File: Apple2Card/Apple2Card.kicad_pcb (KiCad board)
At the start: 2 copper layers, 160 x 78.2 mm, 69 parts, among them J1 ICSP, J2 Conn_01x25, J3 Conn_01x25, J4 Conn_01x16, J5 SERCON, J6 WIZNET 5500, SW1 SW_Push, U1 ATmega328P-P, U2 74HCT32, U3 74HCT00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

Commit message: JLCPCB order 2022-06-15
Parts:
- moved JP10 0.14 mm to (104.4, 34.9)
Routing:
- net GND: track 217.9 -> 241.2 mm
- net Net-(D8-Pad1): track 111.7 -> 112.2 mm
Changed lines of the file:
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@@
       (effects (font (size 1 1) (thickness 0.15)))
     )
-    (fp_text user "K" (at 0 -1.8) (layer "F.Fab")
+    (fp_text user "K" (at 0 -1.8) (layer "F.Fab") hide
       (effects (font (size 1 1) (thickness 0.15)))
     )
@@
   )
   (footprint "Connector_PinHeader_2.54mm:PinHeader_1x02_P2.54mm_Vertical" (layer "F.Cu")
-    (at 104.445 35 90)
+    (at 104.445 34.86 90)
     (descr "Through hole straight pin header, 1x02, 2.54mm pitch, single row")
     (tags "Through hole pin header THT 1x02 2.54mm single row")
@@
   (segment (start 168.59 83.16) (end 115.3 83.16) (width 0.35) (layer "F.Cu") (net 26))
   (segment (start 71.91 63.75) (end 72.64 63.75) (width 0.35) (layer "F.Cu") (net 26))
-  (segment (start 133.79 57.56) (end 137.59 57.56) (width 0.35) (layer "F.Cu") (net 26))
   (segment (start 138.97 58.94) (end 138.97 58.96) (width 0.35) (layer "F.Cu") (net 26))
   (segment (start 69.21 62.36) (end 69.64 61.93) (width 0.35) (layer "F.Cu") (net 26))
   (segment (start 123.12 69.65) (end 123.12 68.23) (width 0.35) (layer "F.Cu") (net 26))
+  (segment (start 135.45 57.56) (end 119.23 57.56) (width 0.35) (layer "F.Cu") (net 26))
   (segment (start 180.09 78.51) (end 178.07 80.53) (width 0.35) (layer "F.Cu") (net 26))
   (segment (start 91.275 72.625) (end 102.2 72.625) (width 0.35) (layer "F.Cu") (net 26))
@@
   (segment (start 108.6 89.86) (end 83.34 89.86) (width 0.35) (layer "F.Cu") (net 26))
   (segment (start 56.73 59.856) (end 58.376 58.21) (width 0.35) (layer "F.Cu") (net 26))
+  (segment (start 119.23 57.56) (end 118.44 56.77) (width 0.35) (layer "F.Cu") (net 26))
   (segment (start 102.2 72.625) (end 103.485 71.34) (width 0.35) (layer "F.Cu") (net 26))
   (segment (start 178.07 80.53) (end 171.22 80.53) (width 0.35) (layer "F.Cu") (net 26))
+  (segment (start 118.44 56.77) (end 118.44 56.56) (width 0.35) (layer "F.Cu") (net 26))
   (segment (start 64.38 57.39) (end 65.55 57.39) (width 0.35) (layer "F.Cu") (net 26))
   (segment (start 138.97 58.96) (end 142.81 62.8) (width 0.35) (layer "F.Cu") (net 26))
+  (segment (start 134.11 57.56) (end 135.45 57.56) (width 0.35) (layer "F.Cu") (net 26))
   (segment (start 121.235 71.535) (end 123.12 69.65) (width 0.35) (layer "F.Cu") (net 26))
   (segment (start 69.64 61.48) (end 71.91 63.75) (width 0.35) (layer "F.Cu") (net 26))
+  (segment (start 135.45 57.56) (end 137.59 57.56) (width 0.35) (layer "F.Cu") (net 26))
   (segment (start 123.12 68.23) (end 133.79 57.56) (width 0.35) (layer "F.Cu") (net 26))
   (segment (start 58.376 58.21) (end 63.56 58.21) (width 0.35) (layer "F.Cu") (net 26))
@@
   (segment (start 103.485 71.34) (end 108.08 71.34) (width 0.35) (layer "F.Cu") (net 26))
   (segment (start 87.1 79.6) (end 87.1 76.8) (width 0.35) (layer "F.Cu") (net 26))
+  (segment (start 133.79 57.56) (end 134.11 57.56) (width 0.35) (layer "F.Cu") (net 26))
   (segment (start 81.82 84.88) (end 87.1 79.6) (width 0.35) (layer "F.Cu") (net 26))
+  (segment (start 118.44 56.56) (end 114.41 52.53) (width 0.35) (layer "F.Cu") (net 26))
   (segment (start 115.3 83.16) (end 108.6 89.86) (width 0.35) (layer "F.Cu") (net 26))
   (segment (start 69.64 61.93) (end 69.64 61.48) (width 0.35) (layer "F.Cu") (net 26))
@@
   (segment (start 43.942 37.2) (end 43.804 37.338) (width 0.35) (layer "B.Cu") (net 55))
   (segment (start 43.804 37.338) (end 40.932 37.338) (width 0.35) (layer "B.Cu") (net 55))
-  (segment (start 117.45 84.81) (end 117.45 84.54) (width 0.35) (layer "F.Cu") (net 56))
-  (segment (start 169.82 83.86) (end 171.23 82.45) (width 0.35) (layer "F.Cu") (net 56))
-  (segment (start 117.45 84.54) (end 118.13 83.86) (width 0.35) (layer "F.Cu") (net 56))
-  (segment (start 118.13 83.86) (end 169.82 83.86) (width 0.35) (layer "F.Cu") (net 56))
-  (via (at 171.23 82.45) (size 0.8) (drill 0.4) (layers "F.Cu" "B.Cu") (net 56))
+  (segment (start 117.45 84.54) (end 117.45 84.81) (width 0.35) (layer "F.Cu") (net 56))
+  (segment (start 118.13 83.86) (end 117.45 84.54) (width 0.35) (layer "F.Cu") (net 56))
+  (segment (start 170.73 83.86) (end 118.13 83.86) (width 0.35) (layer "F.Cu") (net 56))
+  (segment (start 171.2 83.39) (end 170.73 83.86) (width 0.35) (layer "F.Cu") (net 56))
+  (via (at 171.2 83.39) (size 0.8) (drill 0.4) (layers "F.Cu" "B.Cu") (net 56))
   (via (at 117.45 84.81) (size 0.8) (drill 0.4) (layers "F.Cu" "B.Cu") (net 56))
-  (segment (start 187.62 73.14) (end 184.84 73.14) (width 0.35) (layer "B.Cu") (net 56))
+  (segment (start 182.61 75.37) (end 184.84 73.14) (width 0.35) (layer "B.Cu") (net 56))
   (segment (start 101.31 91.89) (end 100.83 92.37) (width 0.35) (layer "B.Cu") (net 56))
-  (segment (start 182.61 75.37) (end 172.99 75.37) (width 0.35) (layer "B.Cu") (net 56))
-  (segment (start 184.84 73.14) (end 182.61 75.37) (width 0.35) (layer "B.Cu") (net 56))
+  (segment (start 171.2 77.16) (end 172.99 75.37) (width 0.35) (layer "B.Cu") (net 56))
+  (segment (start 187.62 73.14) (end 187.62 63.917) (width 0.35) (layer "B.Cu") (net 56))
   (segment (start 117.45 86.6) (end 112.16 91.89) (width 0.35) (layer "B.Cu") (net 56))
   (segment (start 117.45 84.81) (end 117.45 86.6) (width 0.35) (layer "B.Cu") (net 56))
-  (segment (start 185.669 61.966) (end 187.62 63.917) (width 0.35) (layer "B.Cu") (net 56))
-  (segment (start 172.99 75.37) (end 171.2 77.16) (width 0.35) (layer "B.Cu") (net 56))
-  (segment (start 171.2 82.42) (end 171.23 82.45) (width 0.35) (layer "B.Cu") (net 56))
+  (segment (start 184.84 73.14) (end 187.62 73.14) (width 0.35) (layer "B.Cu") (net 56))
+  (segment (start 172.99 75.37) (end 182.61 75.37) (width 0.35) (layer "B.Cu") (net 56))
   (segment (start 112.16 91.89) (end 101.31 91.89) (width 0.35) (layer "B.Cu") (net 56))
-  (segment (start 171.2 77.16) (end 171.2 82.42) (width 0.35) (layer "B.Cu") (net 56))
-  (segment (start 187.62 63.917) (end 187.62 73.14) (width 0.35) (layer "B.Cu") (net 56))
+  (segment (start 171.2 83.39) (end 171.2 77.16) (width 0.35) (layer "B.Cu") (net 56))
+  (segment (start 187.62 63.917) (end 185.669 61.966) (width 0.35) (layer "B.Cu") (net 56))
   (segment (start 100.83 92.37) (end 100.19 92.37) (width 0.35) (layer "B.Cu") (net 56))
   (segment (start 65.02 48.51) (end 60.96 52.57) (width 0.35) (layer "B.Cu") (net 57))
@@
   (segment (start 102.8 29.11) (end 103.59 29.9) (width 0.35) (layer "B.Cu") (net 80))
   (segment (start 92.84 29.8) (end 93.53 29.11) (width 0.35) (layer "B.Cu") (net 80))
-  (segment (start 103.59 34.145) (end 104.445 35) (width 0.35) (layer "B.Cu") (net 80))
+  (segment (start 103.59 34.005) (end 104.445 34.86) (width 0.35) (layer "B.Cu") (net 80))
+  (segment (start 103.59 31.21) (end 103.59 34.005) (width 0.35) (layer "B.Cu") (net 80))
   (segment (start 92.84 38.32) (end 92.84 29.8) (width 0.35) (layer "B.Cu") (net 80))
   (segment (start 93.53 29.11) (end 102.8 29.11) (width 0.35) (layer "B.Cu") (net 80))
-  (segment (start 103.59 31.21) (end 103.59 34.145) (width 0.35) (layer "B.Cu") (net 80))
   (segment (start 103.59 29.9) (end 103.59 31.21) (width 0.35) (layer "B.Cu") (net 80))
   (segment (start 82.906 80.62) (end 91.426 89.14) (width 0.35) (layer "B.Cu") (net 81))
@@
   (segment (start 117.48 36.72) (end 119.44 36.72) (width 0.35) (layer "B.Cu") (net 123))
   (segment (start 119.44 36.72) (end 121.235 38.515) (width 0.35) (layer "B.Cu") (net 123))
-  (segment (start 113.56 34.8) (end 107.185 34.8) (width 0.35) (layer "B.Cu") (net 123))
   (segment (start 113.66 34.7) (end 113.56 34.8) (width 0.35) (layer "B.Cu") (net 123))
-  (segment (start 107.185 34.8) (end 106.985 35) (width 0.35) (layer "B.Cu") (net 123))
+  (segment (start 113.56 34.8) (end 107.045 34.8) (width 0.35) (layer "B.Cu") (net 123))
+  (segment (start 107.045 34.8) (end 106.985 34.86) (width 0.35) (layer "B.Cu") (net 123))
   (segment (start 42.164 48.768) (end 42.214 48.818) (width 0.35) (layer "F.Cu") (net 124))
   (segment (start 45.72 73.96) (end 45.716 73.964) (width 0.35) (layer "F.Cu") (net 124))

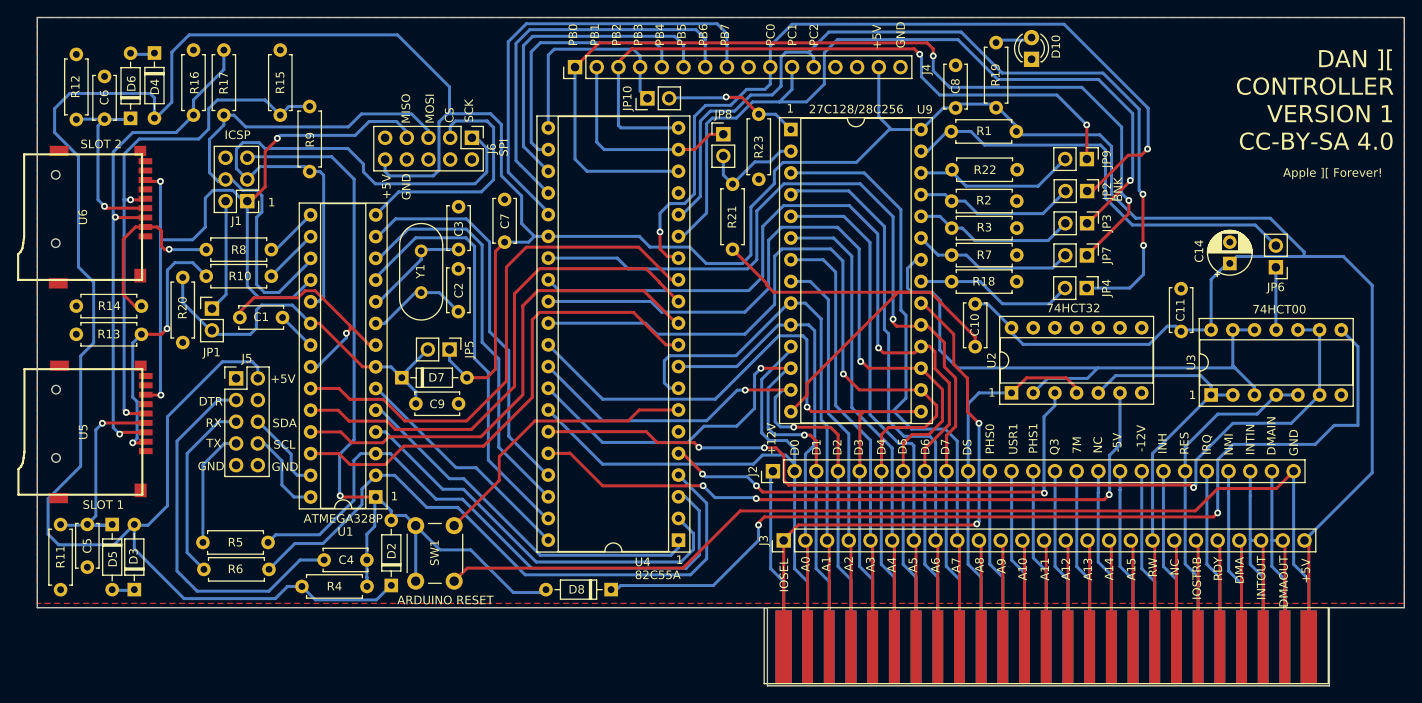
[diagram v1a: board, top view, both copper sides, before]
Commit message: Switched around Ethernet output to front side of card, and added access LED for storage
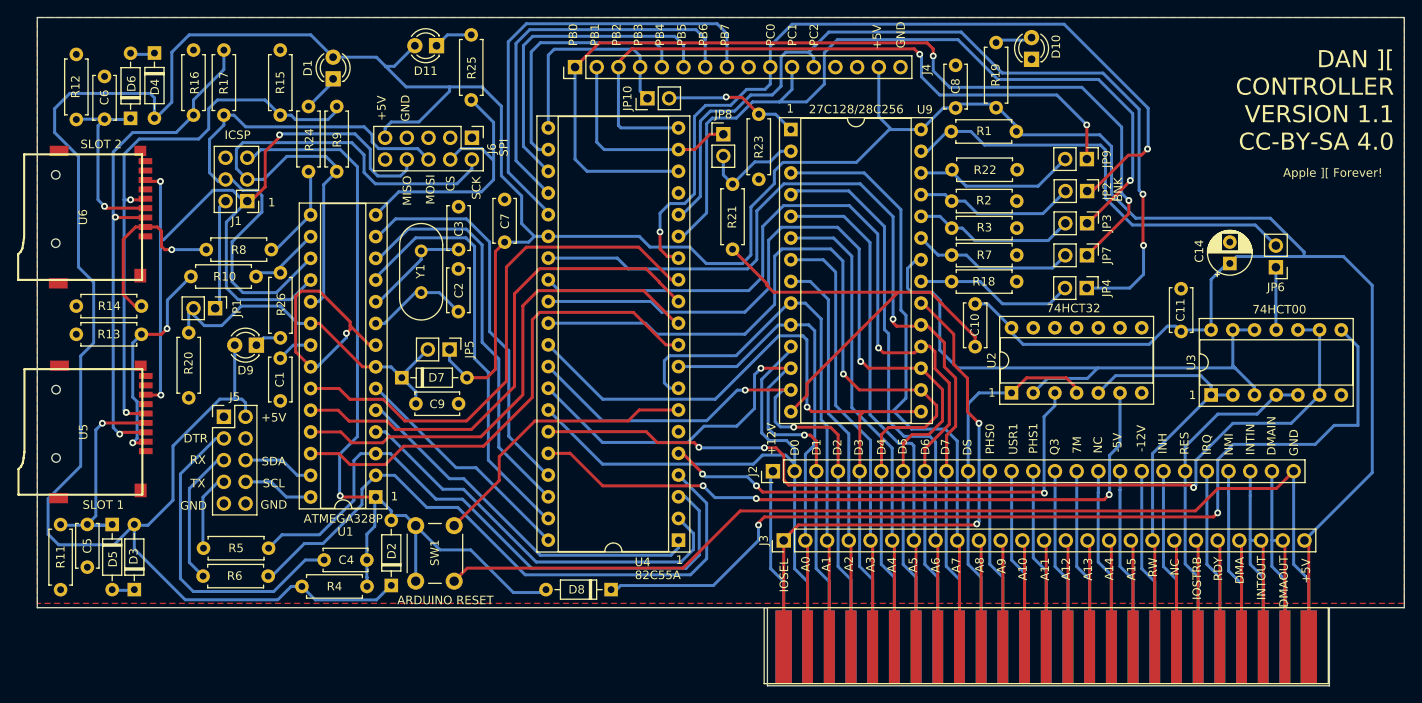
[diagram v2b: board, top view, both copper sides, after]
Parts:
- added D1: LED, LED_THT:LED_D3.0mm, F.Cu at (67.7, 32.6)
- added D11: LED, LED_THT:LED_D3.0mm, F.Cu at (79.8, 28.7)
- added D9: LED, LED_THT:LED_D3.0mm, F.Cu at (58.7, 63.8)
- added R24: 1k, Resistor_THT:R_Axial_DIN0207_L6.3mm_D2.5mm_P7.62mm_Horizontal, F.Cu at (64.8, 35.8)
- added R25: 1k, Resistor_THT:R_Axial_DIN0207_L6.3mm_D2.5mm_P7.62mm_Horizontal, F.Cu at (83.8, 27.4)
- added R26: 1k, Resistor_THT:R_Axial_DIN0207_L6.3mm_D2.5mm_P7.62mm_Horizontal, F.Cu at (61.5, 62.9)
- moved R20 6.51 mm to (50.8, 69.9)
- moved C1 4.77 mm to (61.5, 65.3), turned to -90 degrees
- moved J5 4.72 mm to (54.9, 72.1)
- moved R9 3.16 mm to (68.1, 43.4)
- moved R10 1.79 mm to (58.6, 55.7)
- moved R6 0.80 mm to (52.4, 90.8)
- moved R5 0.67 mm to (52.5, 87.5)
- moved JP1 0.38 mm to (53.8, 59.4), turned to -90 degrees
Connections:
- J6 pad 1: SCK -> unconnected-(J6-Pad1)
- J6 pad 10: +5V -> unconnected-(J6-Pad10)
- J6 pad 2: unconnected-(J6-Pad2) -> SCK
- J6 pad 3: CS3 -> unconnected-(J6-Pad3)
- J6 pad 4: unconnected-(J6-Pad4) -> CS3
- J6 pad 5: MOSI -> unconnected-(J6-Pad5)
- J6 pad 6: unconnected-(J6-Pad6) -> MOSI
- J6 pad 7: MISO -> GND
- J6 pad 8: GND -> MISO
- J6 pad 9: unconnected-(J6-Pad9) -> +5V
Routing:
- net Net-(C4-Pad1): track 43.8 -> 38.0 mm
- net Net-(R6-Pad1): track 21.7 -> 16.3 mm
- net CS2: track 6.28 -> 11.5 mm
- net Net-(R10-Pad2): track 30.8 -> 25.7 mm
- net MISO: track 88.7 -> 93.7 mm
- net Net-(R5-Pad1): track 14.0 -> 9.19 mm
- net Net-(D1-Pad1): track 0.00 -> 4.62 mm
- net Net-(D11-Pad1): track 0.00 -> 4.59 mm
- net Net-(R15-Pad1): track 62.1 -> 66.0 mm
- net MOSI: track 60.9 -> 64.4 mm
- net CS3: track 28.6 -> 32.1 mm
- net Net-(D9-Pad1): track 0.00 -> 3.16 mm
- net Net-(C9-Pad1): track 44.6 -> 41.5 mm
- net CS: track 6.54 -> 8.73 mm
- net RESET: track 98.5 -> 100.6 mm
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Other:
- board text added: "DAN ][ CONTROLLER VERSION 1.1 CC-BY-SA 4.0"
- board text removed: "DAN ][ CONTROLLER VERSION 1 CC-BY-SA 4.0"

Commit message: Added CS/CS2 pins to feature connector
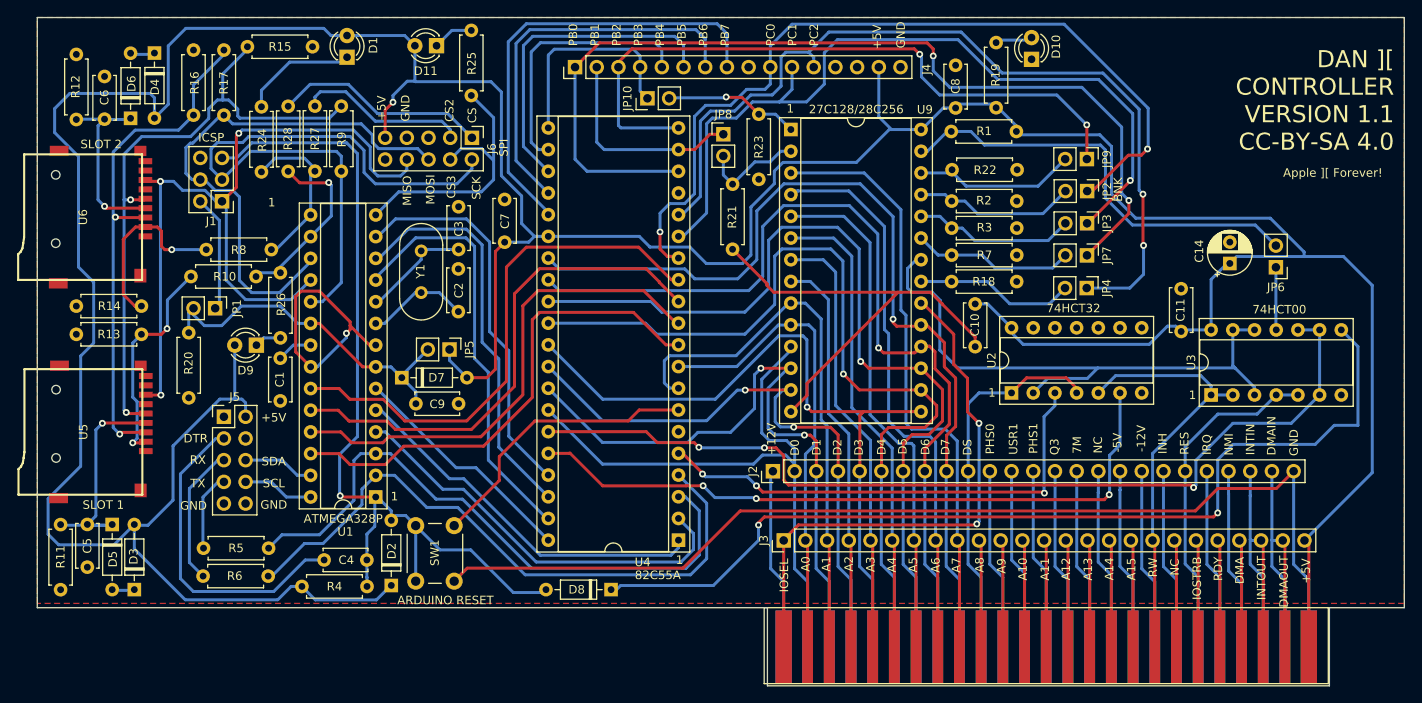
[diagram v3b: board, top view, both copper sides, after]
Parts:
- added R27: 470R, Resistor_THT:R_Axial_DIN0207_L6.3mm_D2.5mm_P7.62mm_Horizontal, F.Cu at (65.5, 43.4)
- added R28: 470R, Resistor_THT:R_Axial_DIN0207_L6.3mm_D2.5mm_P7.62mm_Horizontal, F.Cu at (62.4, 43.4)
- moved R15 8.89 mm to (57.6, 28.8), turned to 0 degrees
- moved R24 5.51 mm to (59.3, 35.9)
- moved D1 3.01 mm to (69.3, 30.1)
- moved J1 2.96 mm to (54.6, 46.9)
- moved R9 0.54 mm to (68.6, 43.4)
- moved R25 0.52 mm to (83.8, 26.9)
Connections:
- J6 pad 1: unconnected-(J6-Pad1) -> Net-(J6-Pad1)
- J6 pad 3: unconnected-(J6-Pad3) -> Net-(J6-Pad3)
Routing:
- net Net-(J6-Pad1): track 0.00 -> 25.2 mm
- net Net-(J6-Pad3): track 0.00 -> 19.9 mm
- net CS: track 8.73 -> 21.5 mm, vias 0 -> 1
- net SCK: track 66.6 -> 75.8 mm
- net Net-(D1-Pad1): track 4.62 -> 13.6 mm
- net CS2: track 11.5 -> 19.3 mm
- net Net-(R15-Pad1): track 66.0 -> 73.3 mm
- net RESET: track 100.6 -> 105.2 mm
- net +5V: track 486.5 -> 484.3 mm, vias 0 -> 1
- net MISO: track 93.7 -> 91.9 mm
- net A7: track 72.2 -> 71.0 mm
- net D7: track 106.7 -> 107.7 mm
- net MOSI: track 64.4 -> 63.6 mm
- net CS3: track 32.1 -> 32.6 mm
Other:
- board text added: "CS2"
- board text added: "CS3"

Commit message: Fixed firmware to work with total replay
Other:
- board text added: "ATMEGA RESET"
- board text removed: "ARDUINO RESET"
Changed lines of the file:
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@@
     (fp_line (start 0.66 -1.25) (end 0.66 1.25) (layer "F.Fab") (width 0.1))
     (fp_line (start 0 0) (end 0.66 0) (layer "F.Fab") (width 0.1))
-    (fp_line (start 6.96 -1.25) (end 0.66 -1.25) (layer "F.Fab") (width 0.1))
     (fp_line (start 0.66 1.25) (end 6.96 1.25) (layer "F.Fab") (width 0.1))
     (fp_line (start 7.62 0) (end 6.96 0) (layer "F.Fab") (width 0.1))
+    (fp_line (start 6.96 -1.25) (end 0.66 -1.25) (layer "F.Fab") (width 0.1))
     (pad "1" thru_hole circle (at 0 0 90) (size 1.6 1.6) (drill 0.8) (layers *.Cu *.Mask)
       (net 64 "CS") (pintype "passive"))
@@
     (effects (font (size 1 1) (thickness 0.15)))
   )
-  (gr_text "ARDUINO RESET" (at 80.8 93.62) (layer "F.SilkS")
+  (gr_text "ATMEGA RESET" (at 80.8 93.62) (layer "F.SilkS")
     (effects (font (size 1 1) (thickness 0.15)))
   )
@@
     (effects (font (size 1 1) (thickness 0.15)))
   )
-  (gr_text "1" (at 60.46 47.05) (layer "F.SilkS")
-    (effects (font (size 1 1) (thickness 0.15)))
-  )
+  (gr_text "1" (at 57.38 47.13) (layer "F.SilkS")
+    (effects (font (size 1 1) (thickness 0.15)))
+  )

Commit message: Fixed issue #5: old pull-up resistor values in PCB design Updated the PCB design with the latest schematics data: the value of the 4k7 pull-ups have changed to 10k, the 470R have changed to 4k7.
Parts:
- R18, R2, R21, R22, R23, R3, R7: value 4k7 -> 10k
- R27, R28: value 470R -> 4k7
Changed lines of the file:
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@@
       (effects (font (size 1 1) (thickness 0.15)))
     )
-    (fp_text value "4k7" (at 3.81 2.37 90) (layer "F.Fab")
+    (fp_text value "10k" (at 3.81 2.37 90) (layer "F.Fab")
       (effects (font (size 1 1) (thickness 0.15)))
     )
@@
       (effects (font (size 1 1) (thickness 0.15)))
     )
-    (fp_text value "4k7" (at 3.81 2.37) (layer "F.Fab")
+    (fp_text value "10k" (at 3.81 2.37) (layer "F.Fab")
       (effects (font (size 1 1) (thickness 0.15)))
     )
@@
       (effects (font (size 1 1) (thickness 0.15)))
     )
-    (fp_text value "4k7" (at 3.81 2.37) (layer "F.Fab")
+    (fp_text value "10k" (at 3.81 2.37) (layer "F.Fab")
       (effects (font (size 1 1) (thickness 0.15)))
     )
@@
       (effects (font (size 1 1) (thickness 0.15)))
     )
-    (fp_text value "470R" (at 3.81 2.37 90) (layer "F.Fab")
+    (fp_text value "4k7" (at 3.81 2.37 90) (layer "F.Fab")
       (effects (font (size 1 1) (thickness 0.15)))
     )
@@
       (effects (font (size 1 1) (thickness 0.15)))
     )
-    (fp_text value "4k7" (at 3.81 2.37) (layer "F.Fab")
+    (fp_text value "10k" (at 3.81 2.37) (layer "F.Fab")
       (effects (font (size 1 1) (thickness 0.15)))
     )
@@
       (effects (font (size 1 1) (thickness 0.15)))
     )
-    (fp_text value "4k7" (at 3.81 2.37 90) (layer "F.Fab")
+    (fp_text value "10k" (at 3.81 2.37 90) (layer "F.Fab")
       (effects (font (size 1 1) (thickness 0.15)))
     )
@@
       (effects (font (size 1 1) (thickness 0.15)))
     )
-    (fp_text value "4k7" (at 3.81 2.37) (layer "F.Fab")
+    (fp_text value "10k" (at 3.81 2.37) (layer "F.Fab")
       (effects (font (size 1 1) (thickness 0.15)))
     )
@@
       (effects (font (size 1 1) (thickness 0.15)))
     )
-    (fp_text value "4k7" (at 3.81 2.37) (layer "F.Fab")
+    (fp_text value "10k" (at 3.81 2.37) (layer "F.Fab")
       (effects (font (size 1 1) (thickness 0.15)))
     )
@@
       (effects (font (size 1 1) (thickness 0.15)))
     )
-    (fp_text value "470R" (at 3.81 2.37 90) (layer "F.Fab")
+    (fp_text value "4k7" (at 3.81 2.37 90) (layer "F.Fab")
       (effects (font (size 1 1) (thickness 0.15)))
     )
